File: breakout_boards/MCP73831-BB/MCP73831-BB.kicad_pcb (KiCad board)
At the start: 2 copper layers, 20.3 x 14.6 mm, 14 parts, among them J1 USB_B_Mini, J2 Conn_01x02, J3 Conn_01x04, U1 MCP73831

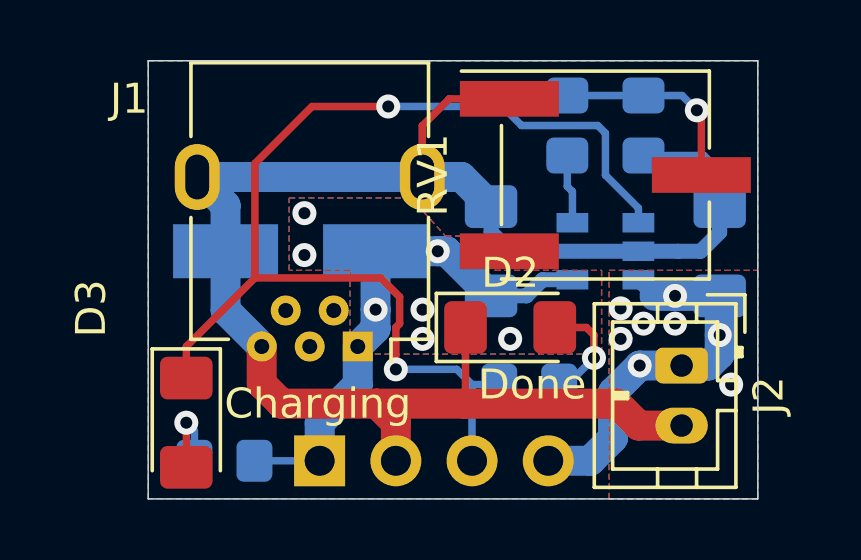
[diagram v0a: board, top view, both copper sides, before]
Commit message: The silk layer is now done. Also added a BOM.
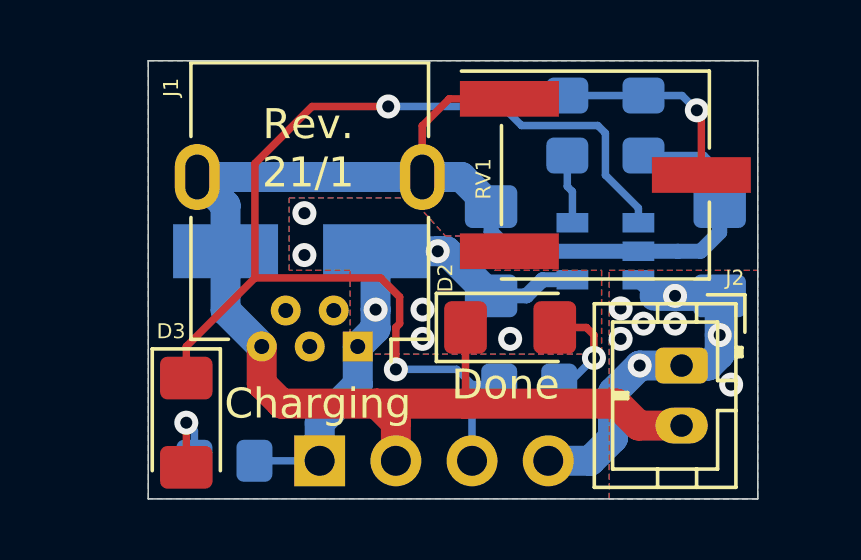
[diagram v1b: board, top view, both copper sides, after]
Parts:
- added REF**: OSHW-Logo_2.7x2.5mm_SilkScreen_NoText, mibe:OSHW-Logo_2.7x2.5mm_SilkScreen_NoText, B.Cu at (105.7, 103.0)
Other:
- board text added: "+"
- board text added: "-"
- board text added: "B"
- board text added: "Rev. 21/1"
- board text added: "S"
- board text added: "mibe.dev"
